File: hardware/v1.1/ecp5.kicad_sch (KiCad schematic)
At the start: 8 parts, among them U1 ECP5U_12_CABGA256

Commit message: Improvements of v1.1
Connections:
- net USB2_PULL: now reaches U1.G16 (PR20A/+/GR_PCLK2_1/HS/RDQS20)
- net USB3_PULL: now reaches U1.H15 (PR20B/-/HS/RDQSN20)
- no-connect marks 50 -> 48
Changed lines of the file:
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@@
 		(title "Icepi zero")
 		(date "2025-05-12")
-		(rev "v1")
+		(rev "v1.1")
 		(company "Chengyin Yao (cheyao)")
 		(comment 1 "https://github.com/cheyao/icepi-zero")
@@
 	)
 	(no_connect
-		(at 214.63 85.09)
-	)
-	(no_connect
 		(at 31.75 163.83)
 	)
@@
 	(no_connect
 		(at 38.1 76.2)
-	)
-	(no_connect
-		(at 214.63 87.63)
 	)
 	(no_connect
@@
 		)
 	)
+	(global_label "USB2_PULL"
+		(shape input)
+		(at 214.63 85.09 180)
+		(fields_autoplaced yes)
+		(effects
+			(font
+				(size 1.27 1.27)
+			)
+			(justify right)
+		)
+		(property "Intersheetrefs" "${INTERSHEET_REFS}"
+			(at 201.001 85.09 0)
+			(effects
+				(font
+					(size 1.27 1.27)
+				)
+				(justify right)
+				(hide yes)
+			)
+		)
+	)
 	(global_label "GPIO_38"
 		(shape input)
@@
 			(effects
 				(font
+					(size 1.27 1.27)
+				)
+				(justify right)
+				(hide yes)
+			)
+		)
+	)
+	(global_label "USB3_PULL"
+		(shape input)
+		(at 214.63 87.63 180)
+		(fields_autoplaced yes)
+		(effects
+			(font
+				(size 1.27 1.27)
+			)
+			(justify right)
+		)
+		(property "Intersheetrefs" "${INTERSHEET_REFS}"
+			(at 201.001 87.63 0)
+			(effects
+				(font

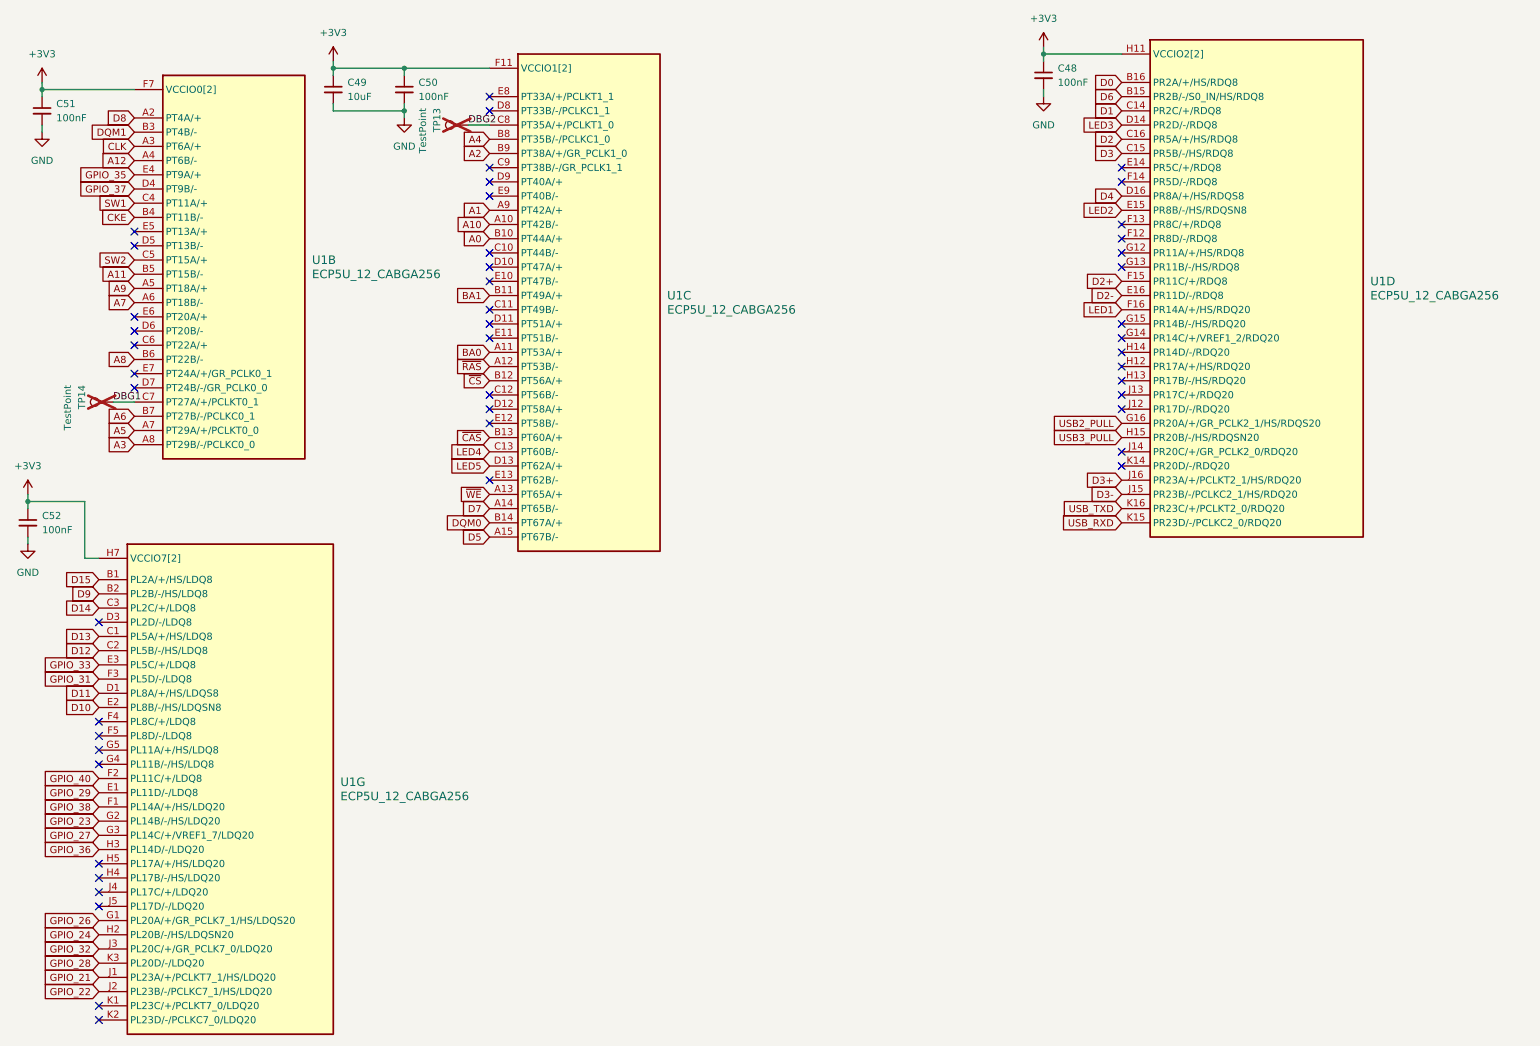
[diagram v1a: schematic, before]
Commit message: Clean up the design by a bit
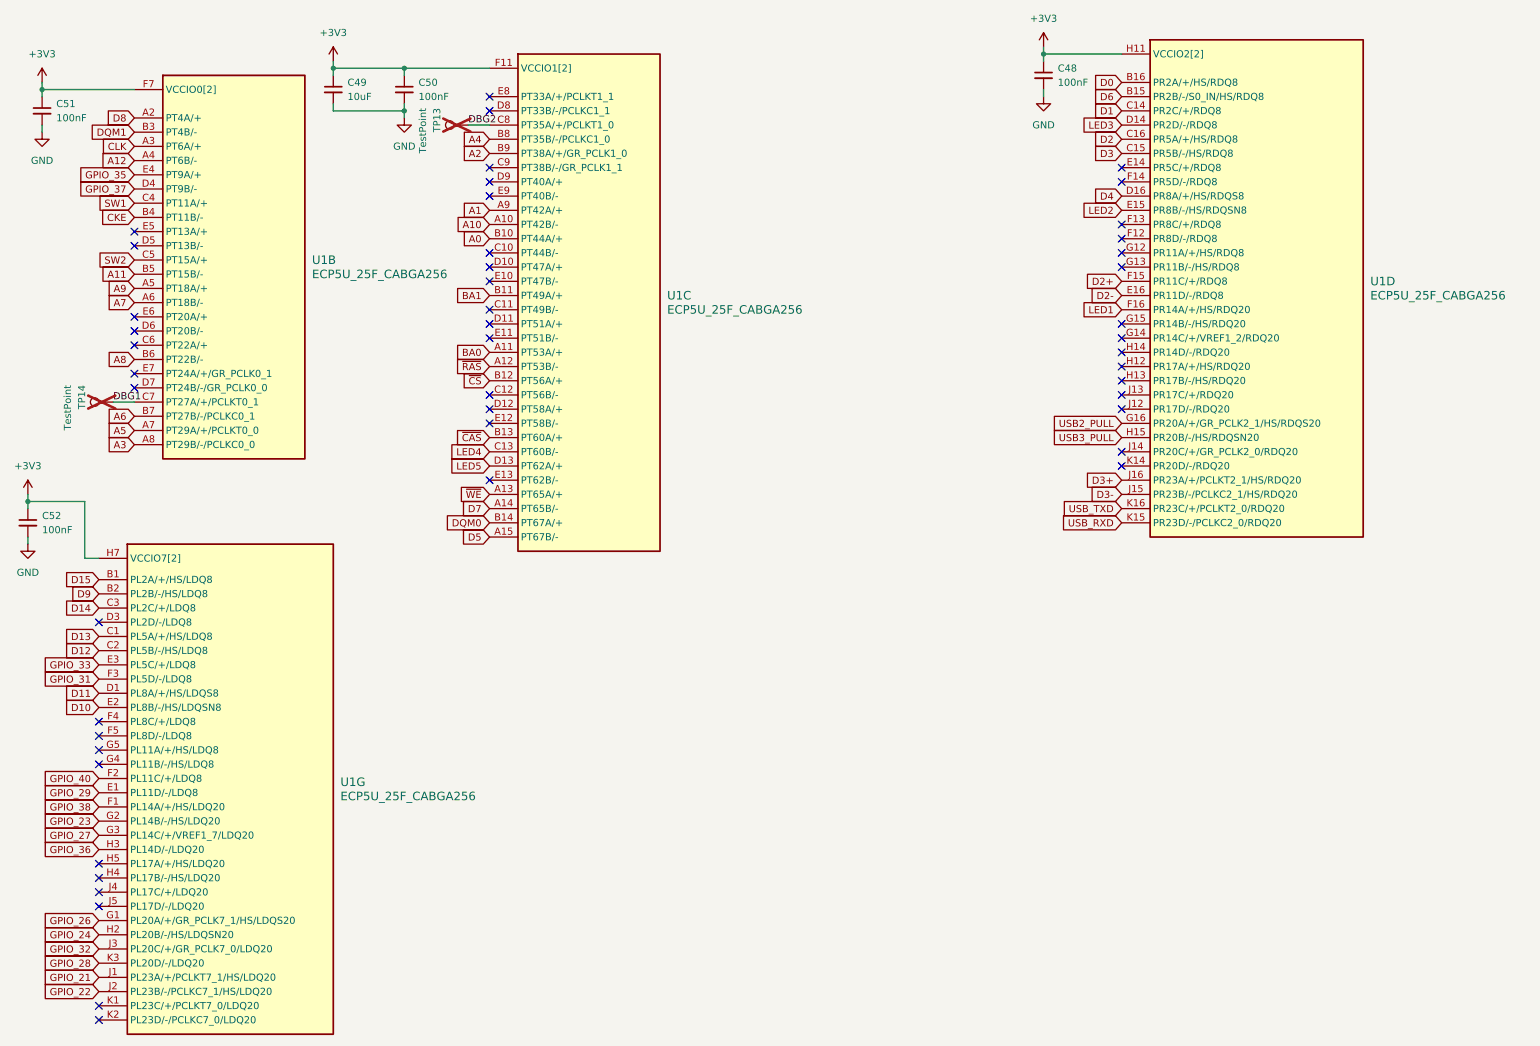
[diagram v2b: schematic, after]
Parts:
- U1: value ECP5U_12_CABGA256 -> ECP5U_25F_CABGA256
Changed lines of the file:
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@@
 			)
 		)
-		(property "Value" "ECP5U_12_CABGA256"
+		(property "Value" "ECP5U_25F_CABGA256"
 			(at 69.85 58.4199 0)
 			(effects
@@
 			)
 		)
-		(property "Value" "ECP5U_12_CABGA256"
+		(property "Value" "ECP5U_25F_CABGA256"
 			(at 259.08 62.2299 0)
 			(effects
@@
 			)
 		)
-		(property "Value" "ECP5U_12_CABGA256"
+		(property "Value" "ECP5U_25F_CABGA256"
 			(at 133.35 64.7699 0)
 			(effects
@@
 			)
 		)
-		(property "Value" "ECP5U_12_CABGA256"
+		(property "Value" "ECP5U_25F_CABGA256"
 			(at 74.93 151.7649 0)
 			(effects

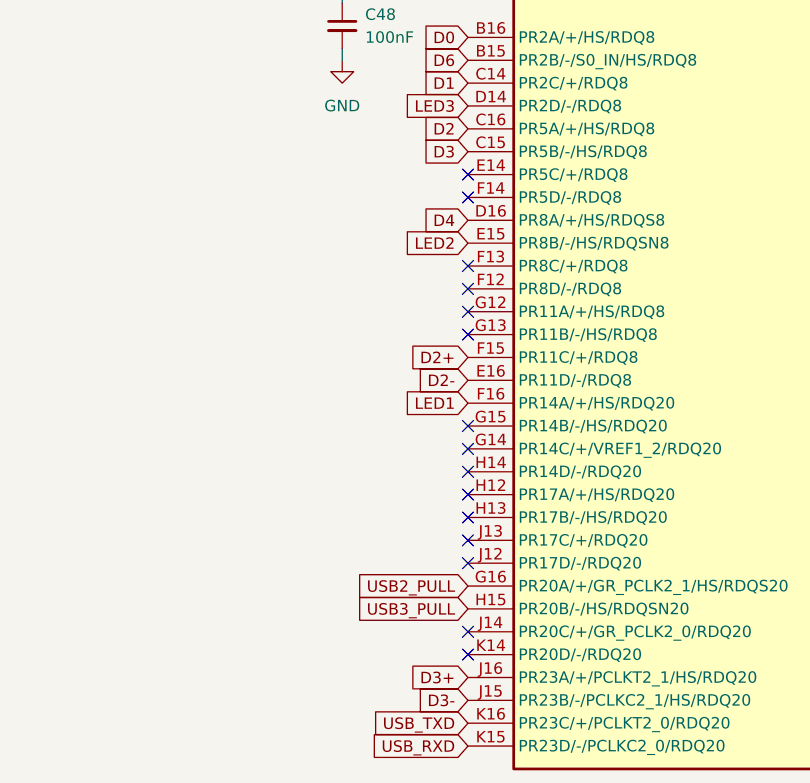
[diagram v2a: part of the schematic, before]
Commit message: Make routing more optimized
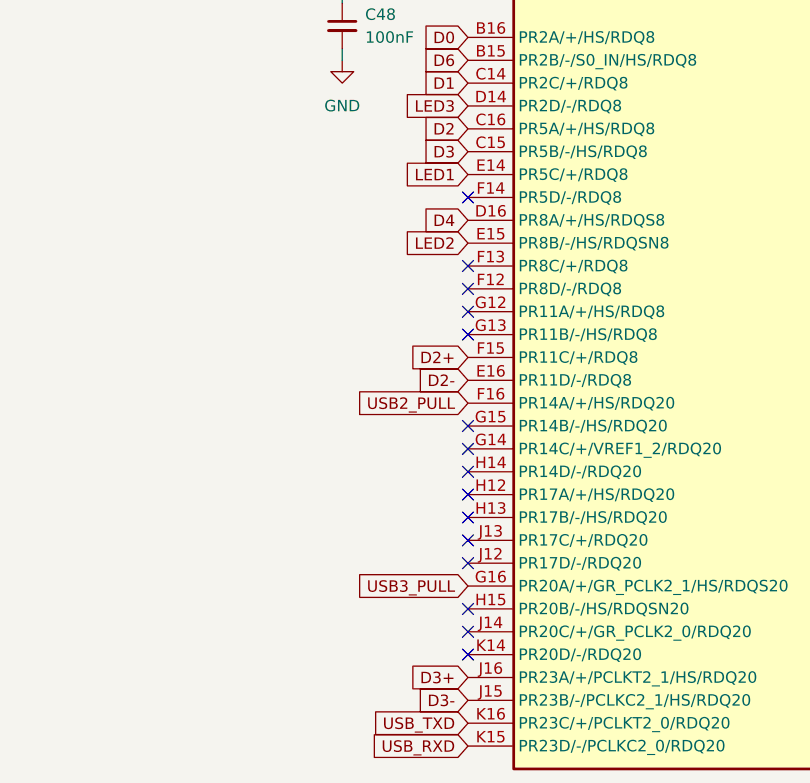
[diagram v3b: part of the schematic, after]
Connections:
- net LED1: now also U1.E14 (PR5C/+/RDQ8); no longer U1.F16 (PR14A/+/HS/RDQ20)
- net USB2_PULL: now also U1.F16 (PR14A/+/HS/RDQ20); no longer U1.G16 (PR20A/+/GR_PCLK2_1/HS/RDQS20)
- net USB3_PULL: now also U1.G16 (PR20A/+/GR_PCLK2_1/HS/RDQS20); no longer U1.H15 (PR20B/-/HS/RDQSN20)
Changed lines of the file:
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@@
 	)
 	(no_connect
-		(at 214.63 39.37)
+		(at 214.63 87.63)
 	)
 	(no_connect
@@
 	(global_label "USB2_PULL"
 		(shape input)
+		(at 214.63 64.77 180)
+		(fields_autoplaced yes)
+		(effects
+			(font
+				(size 1.27 1.27)
+			)
+			(justify right)
+		)
+		(property "Intersheetrefs" "${INTERSHEET_REFS}"
+			(at 201.001 64.77 0)
+			(effects
+				(font
+					(size 1.27 1.27)
+				)
+				(justify right)
+				(hide yes)
+			)
+		)
+	)
+	(global_label "GPIO_38"
+		(shape input)
+		(at 31.75 153.67 180)
+		(fields_autoplaced yes)
+		(effects
+			(font
+				(size 1.27 1.27)
+			)
+			(justify right)
+		)
+		(property "Intersheetrefs" "${INTERSHEET_REFS}"
+			(at 20.9029 153.67 0)
+			(effects
+				(font
+					(size 1.27 1.27)
+				)
+				(justify right)
+				(hide yes)
+			)
+		)
+	)
+	(global_label "A0"
+		(shape input)
+		(at 101.6 52.07 180)
+		(fields_autoplaced yes)
+		(effects
+			(font
+				(size 1.27 1.27)
+			)
+			(justify right)
+		)
+		(property "Intersheetrefs" "${INTERSHEET_REFS}"
+			(at 96.3167 52.07 0)
+			(effects
+				(font
+					(size 1.27 1.27)
+				)
+				(justify right)
+				(hide yes)
+			)
+		)
+	)
+	(global_label "~{CS}"
+		(shape input)
+		(at 101.6 77.47 180)
+		(fields_autoplaced yes)
+		(effects
+			(font
+				(size 1.27 1.27)
+			)
+			(justify right)
+		)
+		(property "Intersheetrefs" "${INTERSHEET_REFS}"
+			(at 96.1353 77.47 0)
+			(effects
+				(font
+					(size 1.27 1.27)
+				)
+				(justify right)
+				(hide yes)
+			)
+		)
+	)
+	(global_label "LED5"
+		(shape input)
+		(at 101.6 92.71 180)
+		(fields_autoplaced yes)
+		(effects
+			(font
+				(size 1.27 1.27)
+			)
+			(justify right)
+		)
+		(property "Intersheetrefs" "${INTERSHEET_REFS}"
+			(at 93.9582 92.71 0)
+			(effects
+				(font
+					(size 1.27 1.27)
+				)
+				(justify right)
+				(hide yes)
+			)
+		)
+	)
+	(global_label "D9"
+		(shape input)
+		(at 31.75 115.57 180)
+		(fields_autoplaced yes)
+		(effects
+			(font
+				(size 1.27 1.27)
+			)
+			(justify right)
+		)
+		(property "Intersheetrefs" "${INTERSHEET_REFS}"
+			(at 26.2853 115.57 0)
+			(effects
+				(font
+					(size 1.27 1.27)
+				)
+				(justify right)
+				(hide yes)
+			)
+		)
+	)
+	(global_label "D2-"
+		(shape input)
+		(at 214.63 62.23 180)
+		(fields_autoplaced yes)
+		(effects
+			(font
+				(size 1.27 1.27)
+			)
+			(justify right)
+		)
+		(property "Intersheetrefs" "${INTERSHEET_REFS}"
+			(at 207.5929 62.23 0)
+			(effects
+				(font
+					(size 1.27 1.27)
+				)
+				(justify right)
+				(hide yes)
+			)
+		)
+	)
+	(global_label "SW1"
+		(shape input)
+		(at 38.1 45.72 180)
+		(fields_autoplaced yes)
+		(effects
+			(font
+				(size 1.27 1.27)
+			)
+			(justify right)
+		)
+		(property "Intersheetrefs" "${INTERSHEET_REFS}"
+			(at 31.2444 45.72 0)
+			(effects
+				(font
+					(size 1.27 1.27)
+				)
+				(justify right)
+				(hide yes)
+			)
+		)
+	)
+	(global_label "CKE"
+		(shape input)
+		(at 38.1 48.26 180)
+		(fields_autoplaced yes)
+		(effects
+			(font
+				(size 1.27 1.27)
+			)
+			(justify right)
+		)
+		(property "Intersheetrefs" "${INTERSHEET_REFS}"
+			(at 31.4258 48.26 0)
+			(effects
+				(font
+					(size 1.27 1.27)
+				)
+				(justify right)
+				(hide yes)
+			)
+		)
+	)
+	(global_label "LED1"
+		(shape input)
+		(at 214.63 39.37 180)
+		(fields_autoplaced yes)
+		(effects
+			(font
+				(size 1.27 1.27)
+			)
+			(justify right)
+		)
+		(property "Intersheetrefs" "${INTERSHEET_REFS}"
+			(at 206.9882 39.37 0)
+			(effects
+				(font
+					(size 1.27 1.27)
+				)
+				(justify right)
+				(hide yes)
+			)
+		)
+	)
+	(global_label "USB3_PULL"
+		(shape input)
 		(at 214.63 85.09 180)
 		(fields_autoplaced yes)
@@
 			(effects
 				(font
-					(size 1.27 1.27)
-				)
-				(justify right)
-				(hide yes)
-			)
-		)
-	)
-	(global_label "GPIO_38"
-		(shape input)
-		(at 31.75 153.67 180)
-		(fields_autoplaced yes)
-		(effects
-			(font
-				(size 1.27 1.27)
-			)
-			(justify right)
-		)
-		(property "Intersheetrefs" "${INTERSHEET_REFS}"
-			(at 20.9029 153.67 0)
-			(effects
-				(font
-					(size 1.27 1.27)
-				)
-				(justify right)
-				(hide yes)
-			)
-		)
-	)
-	(global_label "A0"
-		(shape input)
-		(at 101.6 52.07 180)
-		(fields_autoplaced yes)
-		(effects
-			(font
-				(size 1.27 1.27)
-			)
-			(justify right)
-		)
-		(property "Intersheetrefs" "${INTERSHEET_REFS}"
-			(at 96.3167 52.07 0)
-			(effects
-				(font
-					(size 1.27 1.27)
-				)
-				(justify right)
-				(hide yes)
-			)
-		)
-	)
-	(global_label "~{CS}"
-		(shape input)
-		(at 101.6 77.47 180)
-		(fields_autoplaced yes)
-		(effects
-			(font
-				(size 1.27 1.27)
-			)
-			(justify right)
-		)
-		(property "Intersheetrefs" "${INTERSHEET_REFS}"
-			(at 96.1353 77.47 0)
-			(effects
-				(font
-					(size 1.27 1.27)
-				)
-				(justify right)
-				(hide yes)
-			)
-		)
-	)
-	(global_label "LED5"
-		(shape input)
-		(at 101.6 92.71 180)
-		(fields_autoplaced yes)
-		(effects
-			(font
-				(size 1.27 1.27)
-			)
-			(justify right)
-		)
-		(property "Intersheetrefs" "${INTERSHEET_REFS}"
-			(at 93.9582 92.71 0)
-			(effects
-				(font
-					(size 1.27 1.27)
-				)
-				(justify right)
-				(hide yes)
-			)
-		)
-	)
-	(global_label "D9"
-		(shape input)
-		(at 31.75 115.57 180)
-		(fields_autoplaced yes)
-		(effects
-			(font
-				(size 1.27 1.27)
-			)
-			(justify right)
-		)
-		(property "Intersheetrefs" "${INTERSHEET_REFS}"
-			(at 26.2853 115.57 0)
-			(effects
-				(font
-					(size 1.27 1.27)
-				)
-				(justify right)
-				(hide yes)
-			)
-		)
-	)
-	(global_label "D2-"
-		(shape input)
-		(at 214.63 62.23 180)
-		(fields_autoplaced yes)
-		(effects
-			(font
-				(size 1.27 1.27)
-			)
-			(justify right)
-		)
-		(property "Intersheetrefs" "${INTERSHEET_REFS}"
-			(at 207.5929 62.23 0)
-			(effects
-				(font
-					(size 1.27 1.27)
-				)
-				(justify right)
-				(hide yes)
-			)
-		)
-	)
-	(global_label "SW1"
-		(shape input)
-		(at 38.1 45.72 180)
-		(fields_autoplaced yes)
-		(effects
-			(font
-				(size 1.27 1.27)
-			)
-			(justify right)
-		)
-		(property "Intersheetrefs" "${INTERSHEET_REFS}"
-			(at 31.2444 45.72 0)
-			(effects
-				(font
-					(size 1.27 1.27)
-				)
-				(justify right)
-				(hide yes)
-			)
-		)
-	)
-	(global_label "CKE"
-		(shape input)
-		(at 38.1 48.26 180)
-		(fields_autoplaced yes)
-		(effects
-			(font
-				(size 1.27 1.27)
-			)
-			(justify right)
-		)
-		(property "Intersheetrefs" "${INTERSHEET_REFS}"
-			(at 31.4258 48.26 0)
-			(effects
-				(font
-					(size 1.27 1.27)
-				)
-				(justify right)
-				(hide yes)
-			)
-		)
-	)
-	(global_label "LED1"
-		(shape input)
-		(at 214.63 64.77 180)
-		(fields_autoplaced yes)
-		(effects
-			(font
-				(size 1.27 1.27)
-			)
-			(justify right)
-		)
-		(property "Intersheetrefs" "${INTERSHEET_REFS}"
-			(at 206.9882 64.77 0)
-			(effects
-				(font
-					(size 1.27 1.27)
-				)
-				(justify right)
-				(hide yes)
-			)
-		)
-	)
-	(global_label "USB3_PULL"
-		(shape input)
-		(at 214.63 87.63 180)
-		(fields_autoplaced yes)
-		(effects
-			(font
-				(size 1.27 1.27)
-			)
-			(justify right)
-		)
-		(property "Intersheetrefs" "${INTERSHEET_REFS}"
-			(at 201.001 87.63 0)
-			(effects
-				(font
